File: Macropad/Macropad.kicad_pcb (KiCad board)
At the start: 2 copper layers, 112.2 x 165.1 mm, 81 parts, among them J201 IR_RX, J202 IR_TX, J301 LED_CHAIN, J302 LCD_I2C, J400 BATTERY_LIPO, J401 BAT_CHG_BOOST, J402 USB_C_CHG_IN, SW1 SW_Push, SW10 SW_Push, SW11 SW_Push, SW12 SW_Push, SW13 SW_Push, SW14 SW_Push, SW15 SW_Push, SW16 SW_Push, SW17 SW_Push, SW18 SW_Push, SW19 SW_Push, SW2 SW_Push, SW20 SW_Push, SW21 SW_Push, SW22 SW_Push, SW23 SW_Push, SW24 SW_Push, SW25 SW_Push, SW26 SW_Push, SW3 SW_Push, SW4 SW_Push, SW401 RotaryEncoder_Switch, SW5 SW_Push, SW6 SW_Push, SW7 SW_Push, SW8 SW_Push, SW9 SW_Push, U402 AMS1117-3.3, U403 MCP73831, U404 MT3608, U901 ESP32-S3-WROOM-1-N8R8

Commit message: Project Updates
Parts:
- J201: value IR_RX -> TSOP4838_C124647
- J202: value IR_TX -> IR333-A_C264290
- moved J402 81.1 mm to (51.1, -36.0)
- moved SW401 74.6 mm to (8.00, -10.0)
- moved J302 25.2 mm to (95.0, -18.0)
- moved J202 15.0 mm to (92.2, -28.0)
- moved J201 7.81 mm to (98.2, -28.0)
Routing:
- net USB_CC1: track 3.10 -> 141.2 mm, vias 0 -> 2
- net USB_CC2: track 3.10 -> 126.2 mm, vias 0 -> 2
- net 5V: track 210.3 -> 270.5 mm
- net GND: track 355.1 -> 407.4 mm
- net 3V3: track 137.4 -> 168.7 mm
- net IR_RX: track 20.8 -> 22.6 mm
- net IR_TX: track 21.8 -> 23.2 mm
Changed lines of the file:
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@@
   (footprint "GEN_PinHeader_1x3_P2.54"
     (layer "F.Cu")
-    (at 92.250 -23.000)
+    (at 98.250 -28.000)
     (property "Reference" "J201"
       (at 0 -3 0)
@@
       (effects (font (size 1 1) (thickness 0.15)))
     )
-    (property "Value" "IR_RX"
+    (property "Value" "TSOP4838_C124647"
       (at 0 3 0)
       (layer "F.Fab")
@@
       (net 15 "IR_RX")
     )
-    (model "${KICAD9_3DMODEL_DIR}/Connector_PinHeader_2.54mm.3dshapes/PinHeader_1x03_P2.54mm_Vertical.step"
+    (model "${KICAD9_3DMODEL_DIR}/OptoDevice.3dshapes/Vishay_MINICAST-3Pin.step"
       (offset (xyz 0 0 0))
       (scale (xyz 1 1 1))
@@
   (footprint "GEN_PinHeader_1x3_P2.54"
     (layer "F.Cu")
-    (at 92.250 -13.000)
+    (at 92.250 -28.000)
     (property "Reference" "J202"
       (at 0 -3 0)
@@
       (effects (font (size 1 1) (thickness 0.15)))
     )
-    (property "Value" "IR_TX"
+    (property "Value" "IR333-A_C264290"
       (at 0 3 0)
       (layer "F.Fab")
@@
       (net 14 "IR_TX")
     )
-    (model "${KICAD9_3DMODEL_DIR}/Connector_PinHeader_2.54mm.3dshapes/PinHeader_1x03_P2.54mm_Vertical.step"
+    (model "${KICAD9_3DMODEL_DIR}/LED_THT.3dshapes/LED_D3.0mm.step"
       (offset (xyz 0 0 0))
       (scale (xyz 1 1 1))
@@
   (footprint "GEN_PinHeader_1x4_P2.54"
     (layer "F.Cu")
-    (at 92.250 7.000)
+    (at 95.000 -18.000)
     (property "Reference" "J302"
       (at 0 -3 0)
@@
   (footprint "USB_C_Receptacle_GCT_USB4125_6P_LOCAL"
     (layer "F.Cu")
-    (at 12.000 35.000)
+    (at 51.125 -36.000)
     (property "Reference" "J402"
       (at 0 5.6 0)
@@
   (footprint "GEN_RotaryEncoder_EC11_Switch"
     (layer "F.Cu")
-    (at 78.250 15.000)
+    (at 8.000 -10.000)
     (property "Reference" "SW401"
       (at 0 -8 0)
@@
       (layers "*.Cu" "*.Mask")
     )
+    (model "${KICAD9_3DMODEL_DIR}/MountingHole.3dshapes/MountingHole_3.2mm_M3.step"
+      (offset (xyz 0 0 0))
+      (scale (xyz 1 1 1))
+      (rotate (xyz 0 0 0))
+    )
   )
   (footprint "GEN_MountingHole_3.2mm_M3"
@@
       (layers "*.Cu" "*.Mask")
     )
+    (model "${KICAD9_3DMODEL_DIR}/MountingHole.3dshapes/MountingHole_3.2mm_M3.step"
+      (offset (xyz 0 0 0))
+      (scale (xyz 1 1 1))
+      (rotate (xyz 0 0 0))
+    )
   )
   (footprint "GEN_MountingHole_3.2mm_M3"
@@
       (layers "*.Cu" "*.Mask")
     )
+    (model "${KICAD9_3DMODEL_DIR}/MountingHole.3dshapes/MountingHole_3.2mm_M3.step"
+      (offset (xyz 0 0 0))
+      (scale (xyz 1 1 1))
+      (rotate (xyz 0 0 0))
+    )
   )
   (footprint "GEN_MountingHole_3.2mm_M3"
@@
       (layers "*.Cu" "*.Mask")
     )
+    (model "${KICAD9_3DMODEL_DIR}/MountingHole.3dshapes/MountingHole_3.2mm_M3.step"
+      (offset (xyz 0 0 0))
+      (scale (xyz 1 1 1))
+      (rotate (xyz 0 0 0))
+    )
   )
   (segment
@@
   )
   (segment
-    (start 80.250 -19.190)
-    (end 92.250 -25.540)
-    (width 0.300)
-    (layer "F.Cu")
-    (net 15)
-  )
-  (segment
     (start 80.250 -21.730)
-    (end 92.250 -15.540)
+    (end 92.250 -30.540)
     (width 0.300)
     (layer "F.Cu")
@@
   (via (at 77.155 -12.000) (size 0.800) (drill 0.400) (layers "F.Cu" "B.Cu") (net 11))
   (segment (start 77.155 -12.000) (end 86.250 -14.110) (width 0.250) (layer "B.Cu") (net 11))
-  (segment (start 84.000 -13.020) (end 80.250 -19.190) (width 0.250) (layer "F.Cu") (net 15))
   (segment (start 84.000 -14.290) (end 80.250 -21.730) (width 0.250) (layer "F.Cu") (net 14))
   (segment (start 84.000 -15.560) (end 80.250 -24.270) (width 0.250) (layer "F.Cu") (net 18))
@@
   (segment (start 27.850 14.000) (end 22.250 14.190) (width 0.400) (layer "F.Cu") (net 21))
   (segment (start 27.850 11.700) (end 22.250 10.540) (width 0.400) (layer "F.Cu") (net 23))
-  (segment (start 10.480 31.920) (end 13.520 31.920) (width 0.300) (layer "F.Cu") (net 22))
   (segment (start 13.520 31.920) (end 37.1375 28.950) (width 0.300) (layer "F.Cu") (net 22))
   (segment (start 37.1375 28.950) (end 22.250 16.730) (width 0.300) (layer "F.Cu") (net 22))
@@
   (segment (start 14.750 31.920) (end 22.250 19.270) (width 0.300) (layer "F.Cu") (net 23))
   (segment (start 7.680 32.000) (end 9.250 31.920) (width 0.300) (layer "F.Cu") (net 23))
-  (segment (start 16.320 32.000) (end 14.750 31.920) (width 0.300) (layer "F.Cu") (net 23))
-  (segment (start 7.680 35.800) (end 7.680 32.000) (width 0.300) (layer "F.Cu") (net 23))
-  (segment (start 16.320 35.800) (end 16.320 32.000) (width 0.300) (layer "F.Cu") (net 23))
   (segment (start 11.500 27.175) (end 9.250 31.920) (width 0.250) (layer "F.Cu") (net 23))
   (segment (start 12.500 27.175) (end 14.750 31.920) (width 0.250) (layer "F.Cu") (net 23))
@@
   (segment (start 37.8625 14.950) (end 42.825 18.000) (width 0.250) (layer "F.Cu") (net 55))
   (segment (start 42.825 18.000) (end 41.175 20.000) (width 0.250) (layer "F.Cu") (net 55))
+  (segment (start 84.000 -13.020) (end 98.250 -30.540) (width 0.250) (layer "F.Cu") (net 15))
+  (segment (start 70.250 -11.570) (end 98.250 -25.460) (width 0.250) (layer "B.Cu") (net 21))
+  (segment (start 52.645 -39.080) (end 49.605 -39.080) (width 0.500) (layer "F.Cu") (net 22))
+  (segment (start 52.645 -39.080) (end 92.250 -25.460) (width 0.300) (layer "F.Cu") (net 22))
+  (segment (start 92.250 -25.460) (end 80.250 -11.570) (width 0.300) (layer "F.Cu") (net 22))
+  (segment (start 98.250 -28.000) (end 92.250 -28.000) (width 0.300) (layer "F.Cu") (net 23))
+  (segment (start 98.250 -28.000) (end 80.250 -9.030) (width 0.300) (layer "F.Cu") (net 23))
+  (segment (start 66.500 -28.260) (end 55.445 -35.200) (width 0.300) (layer "F.Cu") (net 23))
+  (segment (start 55.445 -35.200) (end 55.445 -39.000) (width 0.500) (layer "F.Cu") (net 23))
+  (segment (start 55.445 -39.000) (end 53.875 -39.080) (width 0.500) (layer "F.Cu") (net 23))
+  (segment (start 53.875 -39.080) (end 48.375 -39.080) (width 0.500) (layer "F.Cu") (net 23))
+  (segment (start 48.375 -39.080) (end 46.805 -39.000) (width 0.500) (layer "F.Cu") (net 23))
+  (segment (start 46.805 -39.000) (end 46.805 -35.200) (width 0.500) (layer "F.Cu") (net 23))
+  (segment (start 50.625 -39.080) (end 50.625 -37.580) (width 0.250) (layer "F.Cu") (net 51))
+  (via (at 50.625 -37.580) (size 0.800) (drill 0.400) (layers "F.Cu" "B.Cu") (net 51))
+  (segment (start 50.625 -37.580) (end 4.000 -37.580) (width 0.250) (layer "B.Cu") (net 51))
+  (segment (start 4.000 -37.580) (end 4.000 31.920) (width 0.250) (layer "B.Cu") (net 51))
+  (segment (start 4.000 31.920) (end 18.000 31.920) (width 0.250) (layer "B.Cu") (net 51))
+  (via (at 18.000 31.920) (size 0.800) (drill 0.400) (layers "F.Cu" "B.Cu") (net 51))
+  (segment (start 18.000 31.920) (end 11.500 31.920) (width 0.250) (layer "F.Cu") (net 51))
+  (segment (start 51.625 -39.080) (end 51.625 -36.580) (width 0.250) (layer "F.Cu") (net 52))
+  (via (at 51.625 -36.580) (size 0.800) (drill 0.400) (layers "F.Cu" "B.Cu") (net 52))
+  (segment (start 51.625 -36.580) (end 6.000 -36.580) (width 0.250) (layer "B.Cu") (net 52))
+  (segment (start 6.000 -36.580) (end 6.000 31.920) (width 0.250) (layer "B.Cu") (net 52))
+  (segment (start 6.000 31.920) (end 12.500 31.920) (width 0.250) (layer "B.Cu") (net 52))
+  (via (at 12.500 31.920) (size 0.800) (drill 0.400) (layers "F.Cu" "B.Cu") (net 52))
 )

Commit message: finished
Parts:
- added J303: LCD_SPI_CTRL, GEN_PinHeader_1x4_P2.54, F.Cu at (101.0, -18.0)
- added R407: 10k, R_0603_1608Metric_LOCAL, B.Cu at (67.5, -27.0)
- added RGB1: SK6812MINI, RGB_PLACEHOLDER_3535, F.Cu at (9.53, 15.5)
- added RGB10: SK6812MINI, RGB_PLACEHOLDER_3535, F.Cu at (66.7, 58.4)
- added RGB11: SK6812MINI, RGB_PLACEHOLDER_3535, F.Cu at (85.7, 58.4)
- added RGB12: SK6812MINI, RGB_PLACEHOLDER_3535, F.Cu at (9.53, 77.4)
- added RGB13: SK6812MINI, RGB_PLACEHOLDER_3535, F.Cu at (28.6, 77.4)
- added RGB14: SK6812MINI, RGB_PLACEHOLDER_3535, F.Cu at (47.6, 77.4)
- added RGB15: SK6812MINI, RGB_PLACEHOLDER_3535, F.Cu at (66.7, 77.4)
- added RGB16: SK6812MINI, RGB_PLACEHOLDER_3535, F.Cu at (85.7, 77.4)
- added RGB17: SK6812MINI, RGB_PLACEHOLDER_3535, F.Cu at (9.53, 96.5)
- added RGB18: SK6812MINI, RGB_PLACEHOLDER_3535, F.Cu at (28.6, 96.5)
- added RGB19: SK6812MINI, RGB_PLACEHOLDER_3535, F.Cu at (47.6, 96.5)
- added RGB2: SK6812MINI, RGB_PLACEHOLDER_3535, F.Cu at (9.53, 39.3)
- added RGB20: SK6812MINI, RGB_PLACEHOLDER_3535, F.Cu at (66.7, 96.5)
- added RGB21: SK6812MINI, RGB_PLACEHOLDER_3535, F.Cu at (85.7, 96.5)
- added RGB22: SK6812MINI, RGB_PLACEHOLDER_3535, F.Cu at (9.53, 115.5)
- added RGB23: SK6812MINI, RGB_PLACEHOLDER_3535, F.Cu at (28.6, 115.5)
- added RGB24: SK6812MINI, RGB_PLACEHOLDER_3535, F.Cu at (47.6, 115.5)
- added RGB25: SK6812MINI, RGB_PLACEHOLDER_3535, F.Cu at (66.7, 115.5)
- added RGB26: SK6812MINI, RGB_PLACEHOLDER_3535, F.Cu at (85.7, 115.5)
- added RGB3: SK6812MINI, RGB_PLACEHOLDER_3535, F.Cu at (28.6, 39.3)
- added RGB4: SK6812MINI, RGB_PLACEHOLDER_3535, F.Cu at (47.6, 39.3)
- added RGB5: SK6812MINI, RGB_PLACEHOLDER_3535, F.Cu at (66.7, 39.3)
- added RGB6: SK6812MINI, RGB_PLACEHOLDER_3535, F.Cu at (85.7, 39.3)
- added RGB7: SK6812MINI, RGB_PLACEHOLDER_3535, F.Cu at (9.53, 58.4)
- added RGB8: SK6812MINI, RGB_PLACEHOLDER_3535, F.Cu at (28.6, 58.4)
- added RGB9: SK6812MINI, RGB_PLACEHOLDER_3535, F.Cu at (47.6, 58.4)
- added SW402: SW_Push, SW_TACT_3x6_4P_LOCAL, B.Cu at (72.0, -4.00)
- J302: value LCD_I2C -> LCD_SPI_PWRDATA
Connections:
- net LCD_SCL renamed LCD_SCLK
- net LCD_SDA renamed LCD_MOSI
- net LED_DATA renamed RGB_DATA
- U901 pad 3: 3V3 -> EN
- U901 pad 35: (no net) -> HALL_OUT
- U901 pad 36: (no net) -> LCD_CS
- U901 pad 37: (no net) -> LCD_DC
- U901 pad 38: (no net) -> LCD_RST
- U901 pad 39: (no net) -> LCD_BL
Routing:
- net GND: track 407.4 -> 1294.2 mm, vias 0 -> 1
- net 5V: track 270.5 -> 1105.0 mm
- net LED_DIN: track 12.3 -> 110.5 mm
- net RGB6_DOUT: track 0.00 -> 82.0 mm
- net RGB21_DOUT: track 0.00 -> 82.0 mm
- net RGB11_DOUT: track 0.00 -> 82.0 mm
- net RGB16_DOUT: track 0.00 -> 82.0 mm
- net EN: track 0.00 -> 53.7 mm, vias 0 -> 1
- net LCD_SCLK: track 53.8 -> 11.1 mm
- net LCD_MOSI: track 52.6 -> 11.0 mm
- net ENC_SW: track 49.0 -> 87.5 mm, vias 0 -> 1
- net ENC_A: track 56.5 -> 87.3 mm, vias 0 -> 1
- net 3V3: track 168.7 -> 141.0 mm, vias 1 -> 2
- net RGB1_DOUT: track 0.00 -> 25.7 mm
- net ENC_B: track 60.0 -> 84.5 mm, vias 0 -> 1
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
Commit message: fixes
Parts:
- moved R403 72.3 mm to (53.5, -31.5), turned to 0 degrees
- moved R402 70.1 mm to (48.5, -31.5), turned to 0 degrees
- moved U403 24.1 mm to (57.9, 17.9)
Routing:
- net GND: track 1294.2 -> 1321.6 mm
- net CHG_PROG: track 2.04 -> 26.1 mm
- net BAT+: track 55.3 -> 70.8 mm
- net 5V: track 1105.0 -> 1116.9 mm
- net USB_CC1: track 141.2 -> 151.8 mm
- net USB_CC2: track 126.2 -> 134.8 mm

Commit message: DONE DONE DONE
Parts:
- added J304: TOUCH_SD_CTRL, GEN_PinHeader_1x4_P2.54, F.Cu at (72.0, -38.0)
- moved J303 103.1 mm to (-2.00, -23.0), turned to 180 degrees
- moved U402 82.4 mm to (98.0, -34.0)
- moved J301 69.7 mm to (32.0, -38.0), turned to 90 degrees
- moved L401 64.4 mm to (6.00, -38.0)
- moved C403 63.5 mm to (94.0, 27.0)
- moved C404 59.9 mm to (96.0, 33.0)
- moved U404 58.0 mm to (97.0, 12.0)
- moved R406 57.2 mm to (96.0, 39.0)
- moved R404 57.2 mm to (97.0, 22.0)
- moved R405 56.9 mm to (96.0, 36.0)
- moved C402 56.5 mm to (90.0, 27.0)
- moved J401 56.0 mm to (22.0, -38.0), turned to 90 degrees
- moved C405 54.4 mm to (100.0, 33.0)
- moved D401 50.6 mm to (97.0, 7.00)
- moved J400 47.1 mm to (12.0, -38.0), turned to 90 degrees
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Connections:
- U901 pad 24: (no net) -> TOUCH_CS
- U901 pad 25: (no net) -> TOUCH_MISO
- U901 pad 26: (no net) -> TOUCH_IRQ
- U901 pad 27: (no net) -> SD_CS
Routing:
- net GND: track 1321.6 -> 2242.6 mm
- net BAT+: track 70.8 -> 936.4 mm
- net 5V: track 1116.9 -> 1600.4 mm
- net BOOST_SW: track 12.4 -> 483.6 mm
- net BOOST_FB: track 8.42 -> 298.5 mm
- net 3V3: track 141.0 -> 391.2 mm, vias 2 -> 3
- net CHG_PROG: track 26.1 -> 188.9 mm
- net LCD_BL: track 18.9 -> 108.3 mm
- net LCD_RST: track 19.5 -> 106.1 mm
- net LCD_DC: track 20.1 -> 104.0 mm
- net LCD_CS: track 20.7 -> 102.1 mm
- net LED_DIN: track 110.5 -> 157.7 mm
- net SD_CS: track 0.00 -> 32.7 mm
- net TOUCH_IRQ: track 0.00 -> 30.8 mm
- net TOUCH_MISO: track 0.00 -> 28.8 mm
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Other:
- board size 112.2 x 165.1 mm -> 112.2 x 163 mm

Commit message: DONE NOW
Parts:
- J304: value TOUCH_SD_CTRL -> TOUCH_I2C_SD
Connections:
- net TOUCH_CS renamed TOUCH_SDA
- net TOUCH_IRQ renamed TOUCH_SCL
- net TOUCH_MISO renamed SPI_MISO
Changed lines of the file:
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@@
 	(net 86 "LCD_RST")
 	(net 87 "LCD_BL")
-	(net 88 "TOUCH_CS")
-	(net 89 "TOUCH_MISO")
-	(net 90 "TOUCH_IRQ")
+	(net 88 "TOUCH_SDA")
+	(net 89 "SPI_MISO")
+	(net 90 "TOUCH_SCL")
 	(net 91 "SD_CS")
 	(footprint "RGB_PLACEHOLDER_3535"
@@
 			)
 		)
-		(property "Value" "TOUCH_SD_CTRL"
+		(property "Value" "TOUCH_I2C_SD"
 			(at 0 3 0)
 			(layer "F.Fab")
@@
 			(layers "*.Cu" "*.Mask")
 			(remove_unused_layers no)
-			(net 88 "TOUCH_CS")
+			(net 88 "TOUCH_SDA")
 		)
 		(pad "2" thru_hole circle
@@
 			(layers "*.Cu" "*.Mask")
 			(remove_unused_layers no)
-			(net 89 "TOUCH_MISO")
+			(net 89 "SPI_MISO")
 		)
 		(pad "3" thru_hole circle
@@
 			(layers "*.Cu" "*.Mask")
 			(remove_unused_layers no)
-			(net 90 "TOUCH_IRQ")
+			(net 90 "TOUCH_SCL")
 		)
 		(pad "4" thru_hole circle
@@
 			(size 1.5 0.9)
 			(layers "F.Cu" "F.Mask" "F.Paste")
-			(net 88 "TOUCH_CS")
+			(net 88 "TOUCH_SDA")
 		)
 		(pad "25" smd rect
@@
 			(size 1.5 0.9)
 			(layers "F.Cu" "F.Mask" "F.Paste")
-			(net 89 "TOUCH_MISO")
+			(net 89 "SPI_MISO")
 		)
 		(pad "26" smd rect
@@
 			(size 1.5 0.9)
 			(layers "F.Cu" "F.Mask" "F.Paste")
-			(net 90 "TOUCH_IRQ")
+			(net 90 "TOUCH_SCL")
 		)
 		(pad "27" smd rect

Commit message: IR INCREASE
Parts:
- added Q501: AO3400A, SOT-23_LOCAL, F.Cu at (96.5, -24.0)
- added R408: 100R, R_0603_1608Metric_LOCAL, F.Cu at (92.0, -23.0)
- added R409: 100k, R_0603_1608Metric_LOCAL, F.Cu at (94.7, -24.9)
- added R410: 47R, R_0805_2012Metric_LOCAL, F.Cu at (102.1, -24.5)
- J202: value IR333-A_C264290 -> IR_LED_TX_HDR
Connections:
- J202 pad 3: IR_TX -> IR_LED_K
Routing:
- net IR_TX: track 32.2 -> 19.3 mm
- net GND: track 2242.6 -> 2253.6 mm
- net IR_LED_SW: track 0.00 -> 5.65 mm
- net IR_TX_GATE: track 0.00 -> 3.37 mm
- net IR_LED_K: track 0.00 -> 2.81 mm

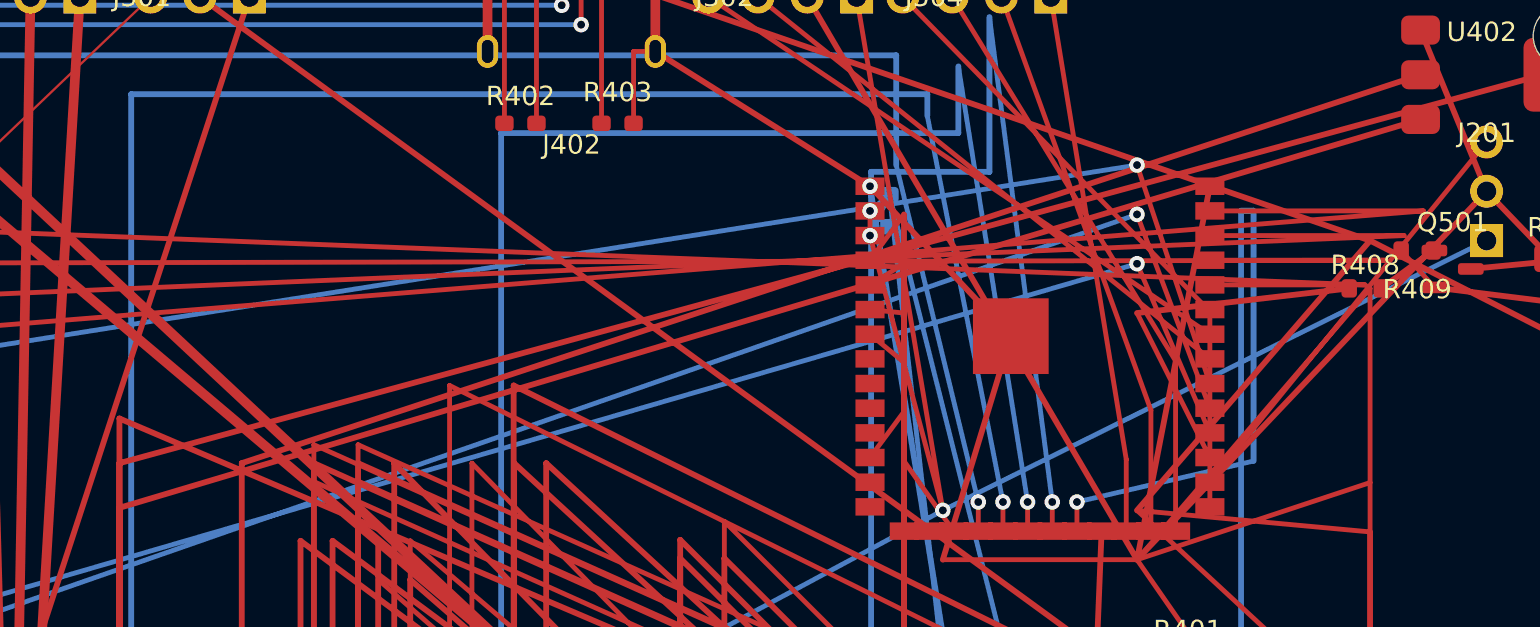
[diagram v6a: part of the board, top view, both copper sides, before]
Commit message: pcb: fix battery/usb power path and charging/boost setpoints
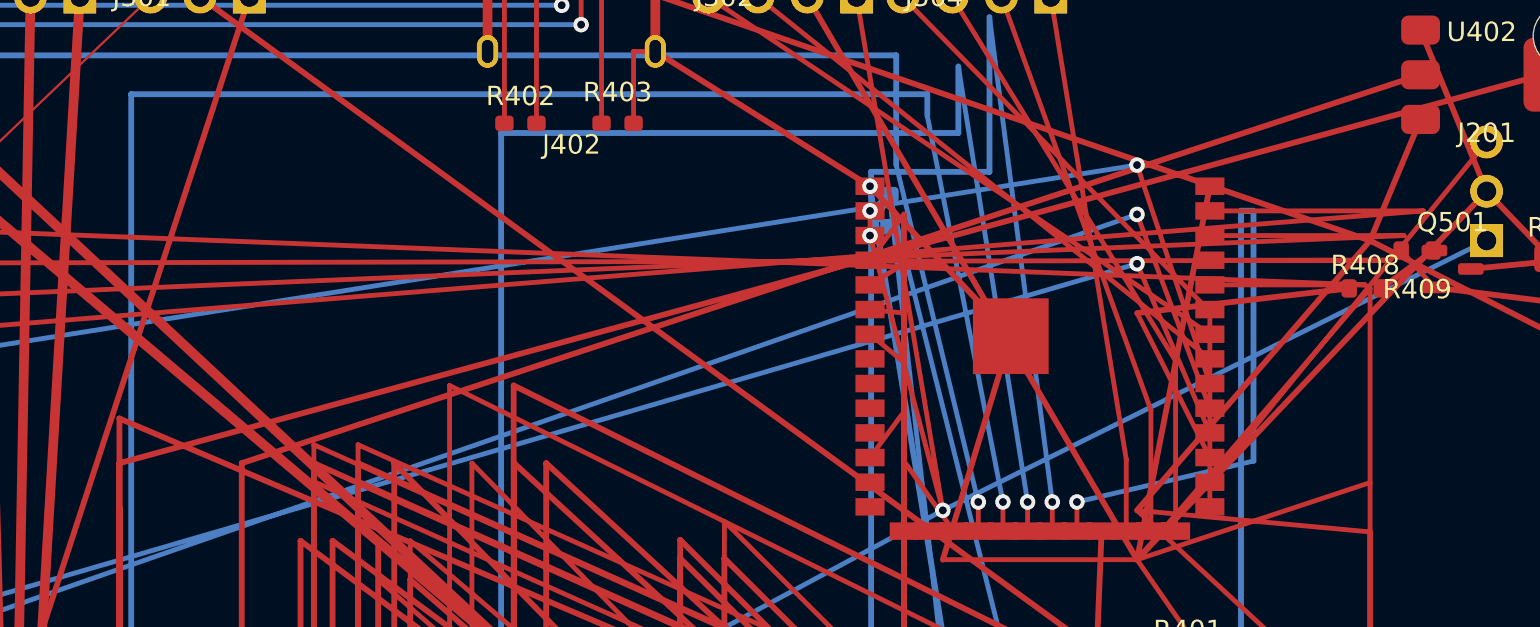
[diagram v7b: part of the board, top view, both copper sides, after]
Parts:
- R404: value 2k -> 3.3k
- R405: value 100k -> 162k
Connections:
- U402 pad 3: BAT+ -> 5V
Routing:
- net BAT+: track 936.4 -> 866.5 mm
- net 5V: track 1600.4 -> 1607.1 mm
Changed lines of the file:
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@@
 			)
 		)
-		(property "Value" "2k"
+		(property "Value" "3.3k"
 			(at 0 1.2 0)
 			(layer "F.Fab")
@@
 			(net 21 "3V3")
 		)
-		(pad "3" smd roundrect
-			(at -3.15 2.3)
-			(size 2 1.5)
-			(layers "F.Cu" "F.Mask" "F.Paste")
-			(roundrect_rratio 0.25)
-			(net 50 "BAT+")
-		)
+			(pad "3" smd roundrect
+				(at -3.15 2.3)
+				(size 2 1.5)
+				(layers "F.Cu" "F.Mask" "F.Paste")
+				(roundrect_rratio 0.25)
+				(net 22 "5V")
+			)
 		(embedded_fonts no)
 		(model "${KICAD9_3DMODEL_DIR}/Package_TO_SOT_SMD.3dshapes/SOT-223.step"
@@
 			)
 		)
-		(property "Value" "100k"
+		(property "Value" "162k"
 			(at 0 1.2 0)
 			(layer "F.Fab")
@@
 	(segment
 		(start 94.85 -31.7)
-		(end 27.85 -11.7)
+		(end 92.25 -25.46)
 		(width 0.3)
 		(layer "F.Cu")
-		(net 50)
+		(net 22)
 	)
 	(segment
